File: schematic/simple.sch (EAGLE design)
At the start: 5 parts, among them IC1 TINY13-20PU

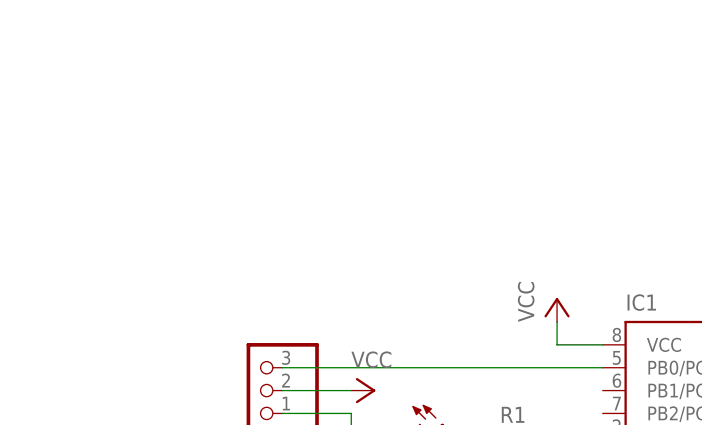
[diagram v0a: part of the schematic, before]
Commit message: added 7805  Regulator for 9V Battery
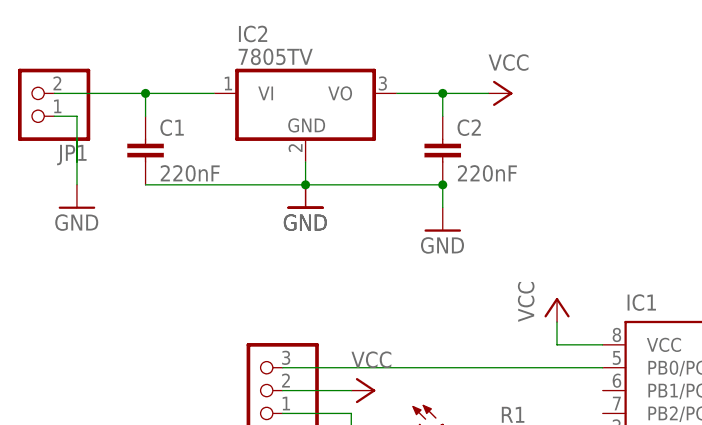
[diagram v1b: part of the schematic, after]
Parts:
- added C1, C2: 220nF, rcl:C-EU025-050X050
- added IC2: 7805TV, linear:7805TV
- added JP1: (no value), pinhead:PINHD-1X2
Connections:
- new net N$5: C1.1, IC2.VI, JP1.2
- new net N$6: JP1.1
- net GND: now also C1.2, C2.2, IC2.GND
- net VCC: now also C2.1, IC2.VO
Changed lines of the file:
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@@
 <part name="R1" library="rcl" deviceset="R-EU_" device="0411/3V"/>
 <part name="OPTIONAL" library="led" deviceset="*P4" device="-BOTTOM" technology="LA"/>
+<part name="IC2" library="linear" deviceset="78*" device="TV" technology="05"/>
+<part name="GND4" library="supply1" deviceset="GND" device=""/>
+<part name="GND5" library="supply1" deviceset="GND" device=""/>
+<part name="JP1" library="pinhead" deviceset="PINHD-1X2" device=""/>
+<part name="C1" library="rcl" deviceset="C-EU" device="025-050X050" value="220nF"/>
+<part name="C2" library="rcl" deviceset="C-EU" device="025-050X050" value="220nF"/>
+<part name="GND6" library="supply1" deviceset="GND" device=""/>
+<part name="GND7" library="supply1" deviceset="GND" device=""/>
+<part name="P+3" library="supply1" deviceset="VCC" device=""/>
 </parts>
 <sheets>
@@
 <instance part="R1" gate="G$1" x="0" y="58.42"/>
 <instance part="OPTIONAL" gate="G$1" x="-10.16" y="58.42" rot="R270"/>
+<instance part="IC2" gate="A1" x="-25.4" y="96.52"/>
+<instance part="GND4" gate="1" x="-25.4" y="83.82"/>
+<instance part="GND5" gate="1" x="-25.4" y="83.82"/>
+<instance part="JP1" gate="G$1" x="-55.88" y="96.52" rot="R180"/>
+<instance part="C1" gate="G$1" x="-43.18" y="91.44"/>
+<instance part="C2" gate="G$1" x="-10.16" y="91.44"/>
+<instance part="GND6" gate="1" x="-50.8" y="83.82"/>
+<instance part="GND7" gate="1" x="-10.16" y="81.28"/>
+<instance part="P+3" gate="VCC" x="-2.54" y="96.52" rot="R270"/>
 </instances>
 <busses>
@@
 <wire x1="-33.02" y1="45.72" x2="-33.02" y2="43.18" width="0.1524" layer="91"/>
 </segment>
+<segment>
+<pinref part="GND4" gate="1" pin="GND"/>
+<pinref part="GND5" gate="1" pin="GND"/>
+<pinref part="IC2" gate="A1" pin="GND"/>
+<wire x1="-25.4" y1="88.9" x2="-25.4" y2="86.36" width="0.1524" layer="91"/>
+<junction x="-25.4" y="86.36"/>
+<pinref part="C1" gate="G$1" pin="2"/>
+<wire x1="-43.18" y1="86.36" x2="-25.4" y2="86.36" width="0.1524" layer="91"/>
+<pinref part="C2" gate="G$1" pin="2"/>
+<wire x1="-25.4" y1="86.36" x2="-10.16" y2="86.36" width="0.1524" layer="91"/>
+<pinref part="GND7" gate="1" pin="GND"/>
+<wire x1="-10.16" y1="86.36" x2="-10.16" y2="83.82" width="0.1524" layer="91"/>
+<junction x="-10.16" y="86.36"/>
+</segment>
 </net>
 <net name="VCC" class="0">
@@
 <pinref part="SERVO" gate="A" pin="2"/>
 <wire x1="-20.32" y1="63.5" x2="-27.94" y2="63.5" width="0.1524" layer="91"/>
+</segment>
+<segment>
+<pinref part="C2" gate="G$1" pin="1"/>
+<wire x1="-10.16" y1="93.98" x2="-10.16" y2="96.52" width="0.1524" layer="91"/>
+<pinref part="IC2" gate="A1" pin="VO"/>
+<wire x1="-10.16" y1="96.52" x2="-15.24" y2="96.52" width="0.1524" layer="91"/>
+<wire x1="-10.16" y1="96.52" x2="-5.08" y2="96.52" width="0.1524" layer="91"/>
+<junction x="-10.16" y="96.52"/>
+<pinref part="P+3" gate="VCC" pin="VCC"/>
 </segment>
 </net>
@@
 </segment>
 </net>
+<net name="N$5" class="0">
+<segment>
+<pinref part="JP1" gate="G$1" pin="2"/>
+<pinref part="IC2" gate="A1" pin="VI"/>
+<wire x1="-53.34" y1="96.52" x2="-43.18" y2="96.52" width="0.1524" layer="91"/>
+<pinref part="C1" gate="G$1" pin="1"/>
+<wire x1="-43.18" y1="96.52" x2="-35.56" y2="96.52" width="0.1524" layer="91"/>
+<wire x1="-43.18" y1="93.98" x2="-43.18" y2="96.52" width="0.1524" layer="91"/>
+<junction x="-43.18" y="96.52"/>
+</segment>
+</net>
+<net name="N$6" class="0">
+<segment>
+<pinref part="JP1" gate="G$1" pin="1"/>
+<wire x1="-53.34" y1="93.98" x2="-50.8" y2="93.98" width="0.1524" layer="91"/>
+<wire x1="-50.8" y1="93.98" x2="-50.8" y2="91.44" width="0.1524" layer="91"/>
+<wire x1="-50.8" y1="91.44" x2="-50.8" y2="88.9" width="0.1524" layer="91"/>
+<wire x1="-50.8" y1="91.44" x2="-50.8" y2="86.36" width="0.1524" layer="91"/>
+</segment>
+</net>
